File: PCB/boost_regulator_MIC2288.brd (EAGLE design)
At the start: 13.2 x 28.2 mm, 13 parts, among them U1 MIC2288YD5-TR

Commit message: Changed resistor values, edited description
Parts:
- R1: value 40K -> 47K
- R2: value 4K7 -> 5K1
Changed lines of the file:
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@@
 <layer number="25" name="tNames" color="7" fill="1" visible="yes" active="yes"/>
 <layer number="26" name="bNames" color="7" fill="1" visible="no" active="yes"/>
-<layer number="27" name="tValues" color="7" fill="1" visible="no" active="yes"/>
+<layer number="27" name="tValues" color="7" fill="1" visible="yes" active="yes"/>
 <layer number="28" name="bValues" color="7" fill="1" visible="no" active="yes"/>
 <layer number="29" name="tStop" color="7" fill="3" visible="no" active="yes"/>
@@
 <attribute name="VALUE" x="9.017" y="22.225" size="1.27" layer="28" rot="MR0"/>
 </element>
-<element name="R1" library="52101-101-REV-A" library_urn="urn:adsk.eagle:library:15662110" package="RC-MASTER-SMD_R0603MP" package3d_urn="urn:adsk.eagle:package:15662272/2" value="40K" x="3.302" y="8.89" smashed="yes" rot="R270">
+<element name="R1" library="52101-101-REV-A" library_urn="urn:adsk.eagle:library:15662110" package="RC-MASTER-SMD_R0603MP" package3d_urn="urn:adsk.eagle:package:15662272/2" value="47K" x="3.302" y="8.89" smashed="yes" rot="R270">
 <attribute name="NAME" x="2.794" y="8.4455" size="0.6096" layer="25" ratio="20" rot="R90"/>
-<attribute name="VALUE" x="3.7465" y="9.3345" size="0.6096" layer="27" ratio="20" rot="R270"/>
+<attribute name="VALUE" x="3.1115" y="11.7475" size="0.6096" layer="27" ratio="20" rot="R270"/>
 </element>
 <element name="R11" library="52101-101-REV-A" library_urn="urn:adsk.eagle:library:15662110" package="RC-MASTER-SMD_R0603MP" package3d_urn="urn:adsk.eagle:package:15662272/2" value="100R" x="9.652" y="6.477" smashed="yes" rot="R90">
@@
 <attribute name="VALUE" x="8.5725" y="7.5565" size="0.6096" layer="27" ratio="20" rot="R270"/>
 </element>
-<element name="R2" library="52101-101-REV-A" library_urn="urn:adsk.eagle:library:15662110" package="RC-MASTER-SMD_R0603MP" package3d_urn="urn:adsk.eagle:package:15662272/2" value="4K7" x="3.302" y="6.35" smashed="yes" rot="R270">
+<element name="R2" library="52101-101-REV-A" library_urn="urn:adsk.eagle:library:15662110" package="RC-MASTER-SMD_R0603MP" package3d_urn="urn:adsk.eagle:package:15662272/2" value="5K1" x="3.302" y="6.35" smashed="yes" rot="R270">
 <attribute name="NAME" x="2.794" y="6.0325" size="0.6096" layer="25" ratio="20" rot="R90"/>
 <attribute name="VALUE" x="3.7465" y="6.7945" size="0.6096" layer="27" ratio="20" rot="R270"/>
@@
 <element name="R3" library="52101-101-REV-A" library_urn="urn:adsk.eagle:library:15662110" package="RC-MASTER-SMD_R0603MP" package3d_urn="urn:adsk.eagle:package:15662272/2" value="1K" x="9.525" y="19.05" smashed="yes" rot="R270">
 <attribute name="NAME" x="10.033" y="19.4945" size="0.6096" layer="25" ratio="20" rot="R270"/>
-<attribute name="VALUE" x="10.6045" y="18.4785" size="0.6096" layer="27" ratio="20" rot="R90"/>
+<attribute name="VALUE" x="9.0805" y="18.6055" size="0.6096" layer="27" ratio="20" rot="R90"/>
 </element>
 <element name="U1" library="MIC2288YD5-TR" library_urn="urn:adsk.eagle:library:23389533" package="SOT95P280X100-5N" package3d_urn="urn:adsk.eagle:package:23389536/2" value="MIC2288YD5-TR" x="6.477" y="8.89" smashed="yes">
@@
 <attribute name="NAME" x="10.033" y="17.653" size="0.6096" layer="25" ratio="20" rot="R270"/>
 <attribute name="POPULARITY" value="26" x="-13.335" y="36.83" size="1.778" layer="27" rot="R180" display="off"/>
-<attribute name="VALUE" x="10.033" y="17.653" size="0.6096" layer="27" ratio="20" rot="R270"/>
+<attribute name="VALUE" x="9.017" y="15.494" size="0.6096" layer="27" ratio="20" rot="R90"/>
 </element>
 <element name="VD2" library="diode" library_urn="urn:adsk.eagle:library:21101624" package="SOD123" package3d_urn="urn:adsk.eagle:package:21101677/2" value="" x="5.969" y="15.875" smashed="yes" rot="R180">

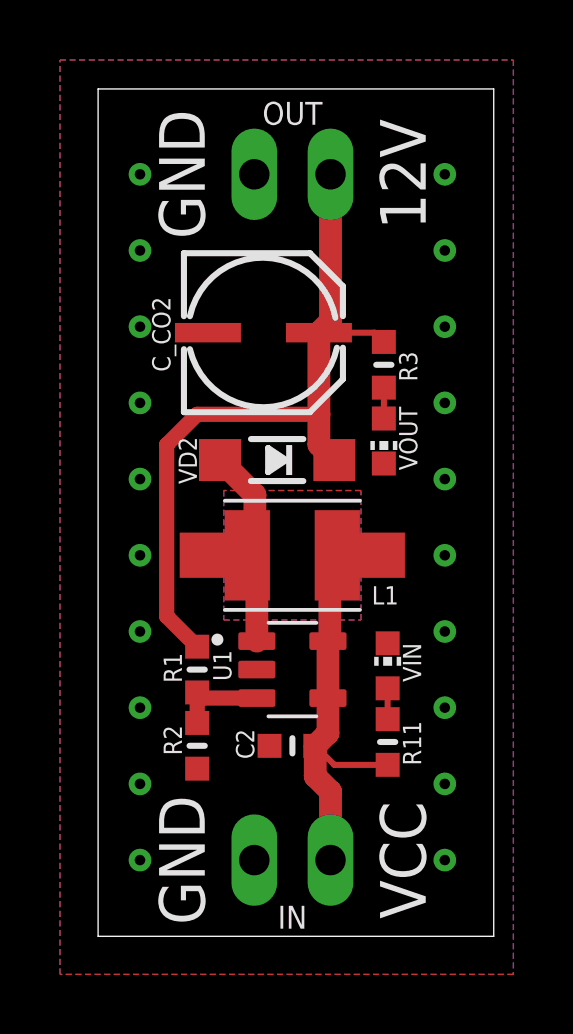
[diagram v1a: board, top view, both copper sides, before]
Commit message: Changed track widths slightly
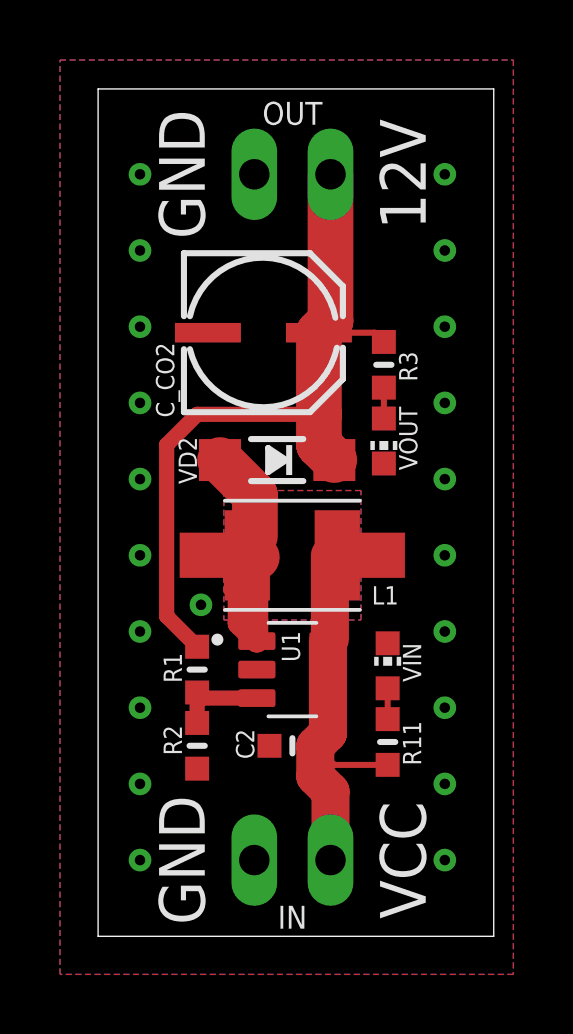
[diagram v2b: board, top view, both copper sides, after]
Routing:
- net N$1: track 6.54 -> 10.6 mm
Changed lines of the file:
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@@
 <layer number="14" name="Route14" color="22" fill="1" visible="no" active="no"/>
 <layer number="15" name="Route15" color="23" fill="1" visible="no" active="no"/>
-<layer number="16" name="Bottom" color="1" fill="1" visible="no" active="yes"/>
+<layer number="16" name="Bottom" color="1" fill="1" visible="yes" active="yes"/>
 <layer number="17" name="Pads" color="2" fill="1" visible="yes" active="yes"/>
 <layer number="18" name="Vias" color="2" fill="1" visible="yes" active="yes"/>
@@
 </element>
 <element name="C_CO2" library="SparkFun-Capacitors" library_urn="urn:adsk.eagle:library:21100215" package="PANASONIC_C" package3d_urn="urn:adsk.eagle:package:21099999/2" value="47uF" x="5.461" y="20.32" smashed="yes">
-<attribute name="NAME" x="2.413" y="20.066" size="0.6096" layer="25" font="vector" ratio="20" rot="R90" align="bottom-center"/>
+<attribute name="NAME" x="2.54" y="18.542" size="0.6096" layer="25" font="vector" ratio="20" rot="R90" align="bottom-center"/>
 <attribute name="PROD_ID" value="CAP-08618" x="21.971" y="-2.54" size="1.778" layer="27" display="off"/>
-<attribute name="VALUE" x="8.382" y="21.717" size="0.6096" layer="27" font="vector" ratio="20" rot="R90" align="top-center"/>
+<attribute name="VALUE" x="9.017" y="21.717" size="0.6096" layer="27" font="vector" ratio="20" rot="R270" align="top-center"/>
 </element>
 <element name="INPUT" library="pinhead" library_urn="urn:adsk.eagle:library:325" package="1X02" package3d_urn="urn:adsk.eagle:package:22435/2" value="" x="6.477" y="2.54" smashed="yes" rot="MR0">
@@
 <element name="R1" library="52101-101-REV-A" library_urn="urn:adsk.eagle:library:15662110" package="RC-MASTER-SMD_R0603MP" package3d_urn="urn:adsk.eagle:package:15662272/2" value="47K" x="3.302" y="8.89" smashed="yes" rot="R270">
 <attribute name="NAME" x="2.794" y="8.4455" size="0.6096" layer="25" ratio="20" rot="R90"/>
-<attribute name="VALUE" x="3.1115" y="11.7475" size="0.6096" layer="27" ratio="20" rot="R270"/>
+<attribute name="VALUE" x="3.7465" y="9.4615" size="0.6096" layer="27" ratio="20" rot="R270"/>
 </element>
 <element name="R11" library="52101-101-REV-A" library_urn="urn:adsk.eagle:library:15662110" package="RC-MASTER-SMD_R0603MP" package3d_urn="urn:adsk.eagle:package:15662272/2" value="100R" x="9.652" y="6.477" smashed="yes" rot="R90">
@@
 <attribute name="MF" value="Microchip Technology" x="31.877" y="3.81" size="1.778" layer="27" display="off"/>
 <attribute name="MP" value="MIC2288YD5-TR" x="31.877" y="3.81" size="1.778" layer="27" display="off"/>
-<attribute name="NAME" x="4.445" y="8.509" size="0.6096" layer="25" ratio="20" rot="R90"/>
+<attribute name="NAME" x="6.731" y="9.144" size="0.6096" layer="25" ratio="20" rot="R90"/>
 <attribute name="PACKAGE" value="None" x="31.877" y="3.81" size="1.778" layer="27" display="off"/>
 <attribute name="PRICE" value="None" x="31.877" y="3.81" size="1.778" layer="27" display="off"/>
@@
 <via x="1.397" y="5.08" extent="1-16" drill="0.35"/>
 <via x="1.397" y="2.54" extent="1-16" drill="0.35"/>
+<via x="3.429" y="11.049" extent="1-16" drill="0.35"/>
 </signal>
 <signal name="ACTIVITY">
@@
 <contactref element="C2" pad="1"/>
 <contactref element="R11" pad="1"/>
-<wire x1="7.727" y1="12.7" x2="7.727" y2="9.905" width="0.762" layer="1"/>
+<wire x1="7.727" y1="12.7" x2="7.727" y2="9.905" width="1.27" layer="1"/>
 <wire x1="7.727" y1="9.905" x2="7.662" y2="9.84" width="0.762" layer="1"/>
-<wire x1="7.662" y1="9.84" x2="7.662" y2="7.94" width="0.762" layer="1"/>
-<wire x1="7.662" y1="7.94" x2="7.662" y2="6.773" width="0.762" layer="1"/>
-<wire x1="7.662" y1="6.773" x2="7.239" y2="6.35" width="0.762" layer="1"/>
-<wire x1="7.239" y1="6.35" x2="7.239" y2="5.334" width="0.762" layer="1"/>
-<wire x1="7.747" y1="4.826" x2="7.239" y2="5.334" width="0.762" layer="1"/>
+<wire x1="7.662" y1="9.84" x2="7.662" y2="7.94" width="1.27" layer="1"/>
+<wire x1="7.662" y1="7.94" x2="7.662" y2="6.773" width="1.27" layer="1"/>
+<wire x1="7.662" y1="6.773" x2="7.239" y2="6.35" width="1.27" layer="1"/>
+<wire x1="7.239" y1="6.35" x2="7.239" y2="5.334" width="1.27" layer="1"/>
+<wire x1="7.747" y1="4.826" x2="7.239" y2="5.334" width="1.27" layer="1"/>
 <wire x1="9.652" y1="5.715" x2="7.874" y2="5.715" width="0.2032" layer="1"/>
 <wire x1="7.874" y1="5.715" x2="7.239" y2="6.35" width="0.2032" layer="1"/>
-<wire x1="7.747" y1="2.54" x2="7.747" y2="4.826" width="0.762" layer="1"/>
+<wire x1="7.747" y1="2.54" x2="7.747" y2="4.826" width="1.27" layer="1"/>
 </signal>
 <signal name="VCC/2">
@@
 <contactref element="R1" pad="1"/>
 <contactref element="C_CO2" pad="+"/>
-<wire x1="7.747" y1="20.506" x2="7.361" y2="20.12" width="0.762" layer="1"/>
-<wire x1="7.361" y1="20.12" x2="7.361" y2="17.399" width="0.762" layer="1"/>
+<wire x1="7.747" y1="20.506" x2="7.361" y2="20.12" width="1.524" layer="1"/>
+<wire x1="7.361" y1="20.12" x2="7.361" y2="17.399" width="1.524" layer="1"/>
 <wire x1="3.302" y1="9.652" x2="2.286" y2="10.668" width="0.508" layer="1"/>
 <wire x1="3.302" y1="17.399" x2="7.361" y2="17.399" width="0.508" layer="1"/>
@@
 <wire x1="9.217" y1="20.12" x2="9.525" y2="19.812" width="0.2032" layer="1"/>
 <contactref element="VD2" pad="C"/>
-<wire x1="7.747" y1="25.4" x2="7.747" y2="20.506" width="0.762" layer="1"/>
-<wire x1="7.874" y1="15.875" x2="7.361" y2="16.388" width="0.762" layer="1"/>
-<wire x1="7.361" y1="16.388" x2="7.361" y2="17.399" width="0.762" layer="1"/>
+<wire x1="7.747" y1="25.4" x2="7.747" y2="20.506" width="1.524" layer="1"/>
+<wire x1="7.874" y1="15.875" x2="7.361" y2="16.388" width="1.524" layer="1"/>
+<wire x1="7.361" y1="16.388" x2="7.361" y2="17.399" width="1.524" layer="1"/>
 </signal>
 <signal name="N$1">
@@
 <contactref element="U1" pad="1"/>
 <contactref element="VD2" pad="A"/>
-<wire x1="4.064" y1="15.875" x2="5.227" y2="14.712" width="0.762" layer="1"/>
-<wire x1="5.227" y1="14.712" x2="5.227" y2="12.7" width="0.762" layer="1"/>
+<wire x1="4.064" y1="15.875" x2="5.227" y2="14.712" width="1.524" layer="1"/>
+<wire x1="5.227" y1="14.712" x2="5.227" y2="13.335" width="1.524" layer="1"/>
+<wire x1="5.227" y1="13.335" x2="5.227" y2="12.7" width="1.143" layer="1"/>
 <wire x1="5.292" y1="9.84" x2="5.292" y2="12.635" width="0.762" layer="1"/>
-<wire x1="5.292" y1="12.635" x2="5.227" y2="12.7" width="0.762" layer="1"/>
+<wire x1="5.292" y1="12.635" x2="5.227" y2="12.7" width="1.524" layer="1"/>
+<wire x1="5.292" y1="9.84" x2="4.699" y2="10.433" width="0.762" layer="1"/>
+<wire x1="4.699" y1="11.43" x2="4.572" y2="11.557" width="0.762" layer="1"/>
+<wire x1="4.572" y1="12.68" x2="5.227" y2="13.335" width="0.762" layer="1"/>
+<wire x1="4.699" y1="10.433" x2="4.699" y2="11.43" width="0.762" layer="1"/>
+<wire x1="4.572" y1="11.557" x2="4.572" y2="12.68" width="0.762" layer="1"/>
 </signal>
 <signal name="N$3">
